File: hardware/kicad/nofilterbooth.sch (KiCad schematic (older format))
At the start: 2 parts

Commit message: kicad schematic & pcb v0.1
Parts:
- CONN_POWER_IN1: symbol nofilterbooth:Conn_01x02-Connector_Generic -> 1nofilterbooth:Conn_01x02-Connector_Generic
- U_STEP_DOWN_5V1: footprint kicadlib:D24V90F5 -> 1nofilterbooth:D24V90F5; symbol nofilterbooth:D24V90F5 -> 1nofilterbooth:D24V90F5
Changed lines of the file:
@@
 $EndSheet
 $Comp
-L nofilterbooth:Conn_01x02-Connector_Generic CONN_POWER_IN1
+L 1nofilterbooth:Conn_01x02-Connector_Generic CONN_POWER_IN1
 U 1 1 5E43D742
 P 4075 1075
@@
 $EndComp
 $Comp
-L nofilterbooth:+12V-power #PWR0123
+L 1nofilterbooth:+12V-power #PWR0123
 U 1 1 5E3BF560
 P 4075 1275
@@
 $EndComp
 $Comp
-L nofilterbooth:GND-power #PWR0124
+L 1nofilterbooth:GND-power #PWR0124
 U 1 1 5E3C03FE
 P 4175 1275
@@
 $EndComp
 $Comp
-L nofilterbooth:D24V90F5 U_STEP_DOWN_5V1
+L 1nofilterbooth:D24V90F5 U_STEP_DOWN_5V1
 U 1 1 5E3C0E82
 P 6000 1125
 F 0 "U_STEP_DOWN_5V1" H 5675 975 50  0000 C CNN
 F 1 "D24V90F5" H 5725 825 50  0000 C CNN
-F 2 "kicadlib:D24V90F5" H 6000 1125 50  0001 C CNN
+F 2 "1nofilterbooth:D24V90F5" H 6000 1125 50  0001 C CNN
 F 3 "" H 6000 1125 50  0001 C CNN
 	1    6000 1125
@@
 $EndComp
 $Comp
-L nofilterbooth:+5V-power #PWR0128
+L 1nofilterbooth:+5V-power #PWR0128
 U 1 1 5E3C178D
 P 6200 1225
@@
 $EndComp
 $Comp
-L nofilterbooth:GND-power #PWR0126
+L 1nofilterbooth:GND-power #PWR0126
 U 1 1 5E3C0BAF
 P 6200 1425
@@
 $EndComp
 $Comp
-L nofilterbooth:GND-power #PWR0125
+L 1nofilterbooth:GND-power #PWR0125
 U 1 1 5E3BFE89
 P 5200 1425
@@
 $EndSheet
 $Comp
-L nofilterbooth:+12V-power #PWR0127
+L 1nofilterbooth:+12V-power #PWR0127
 U 1 1 5E3DD7DE
 P 5200 1225

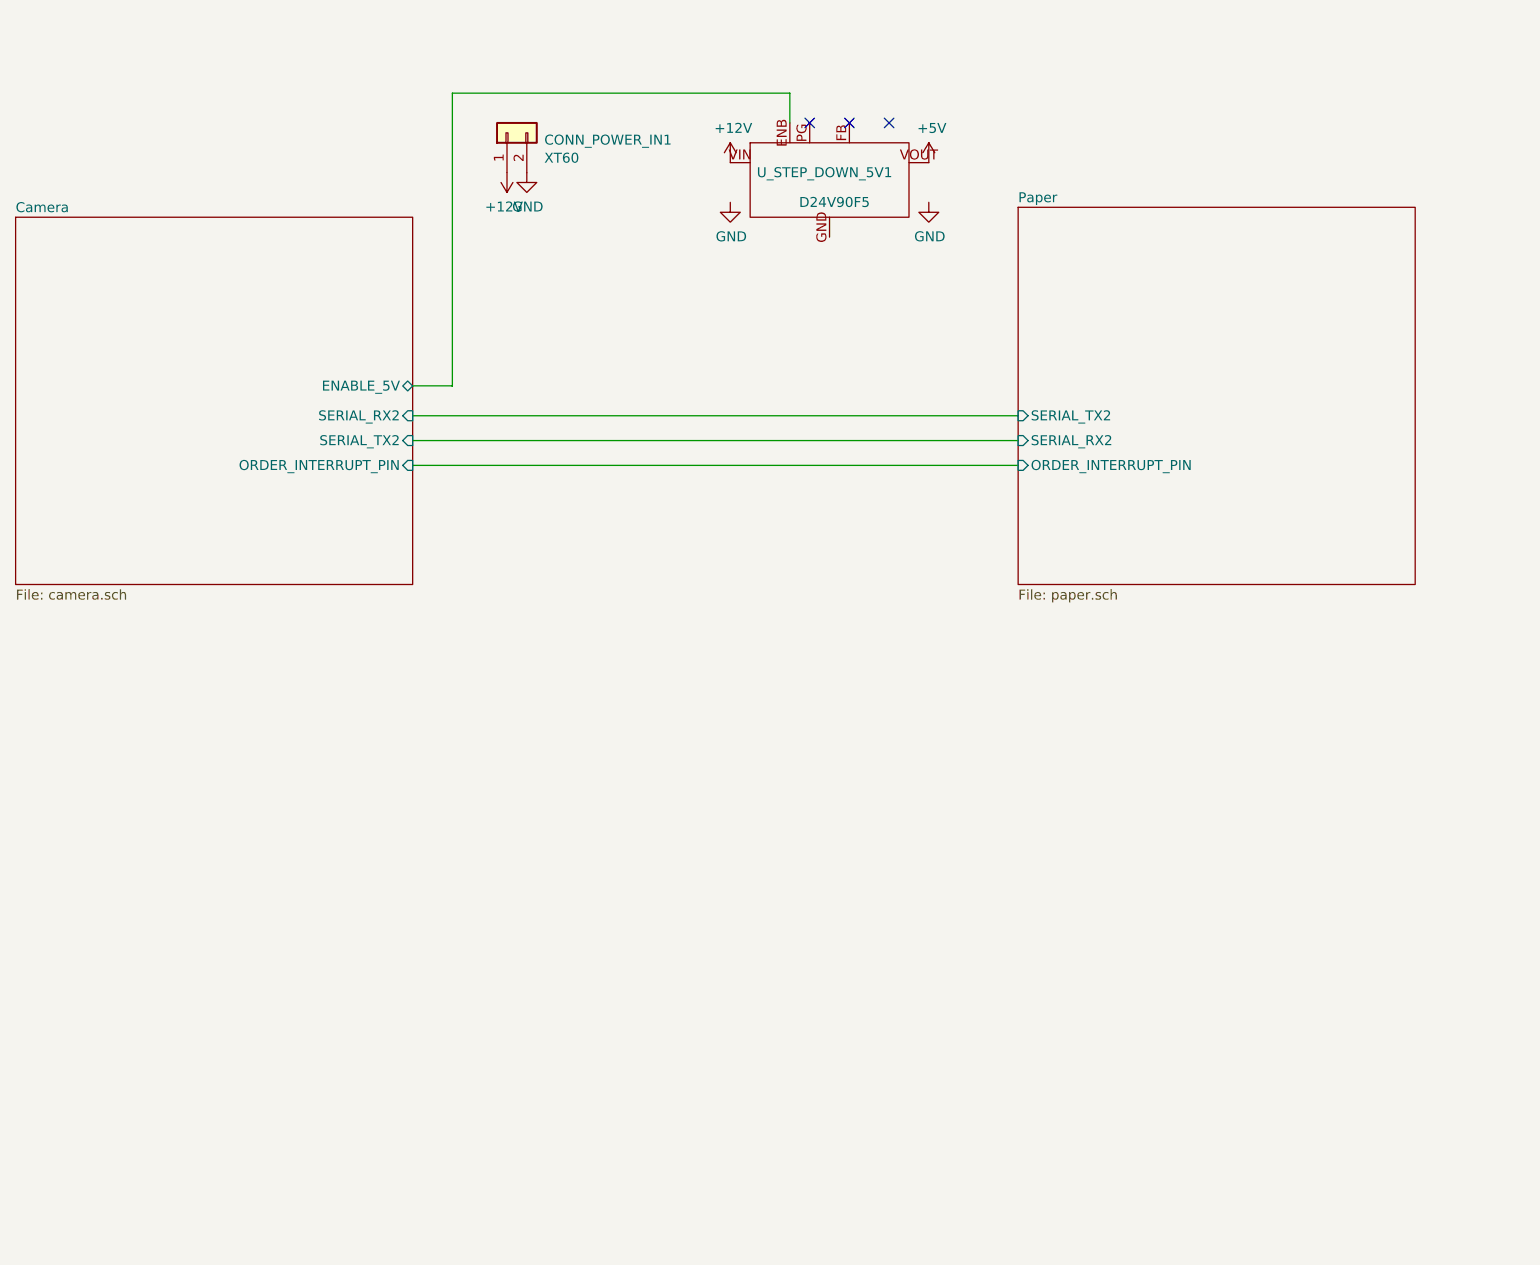
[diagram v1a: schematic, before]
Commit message: correction schematic gilou
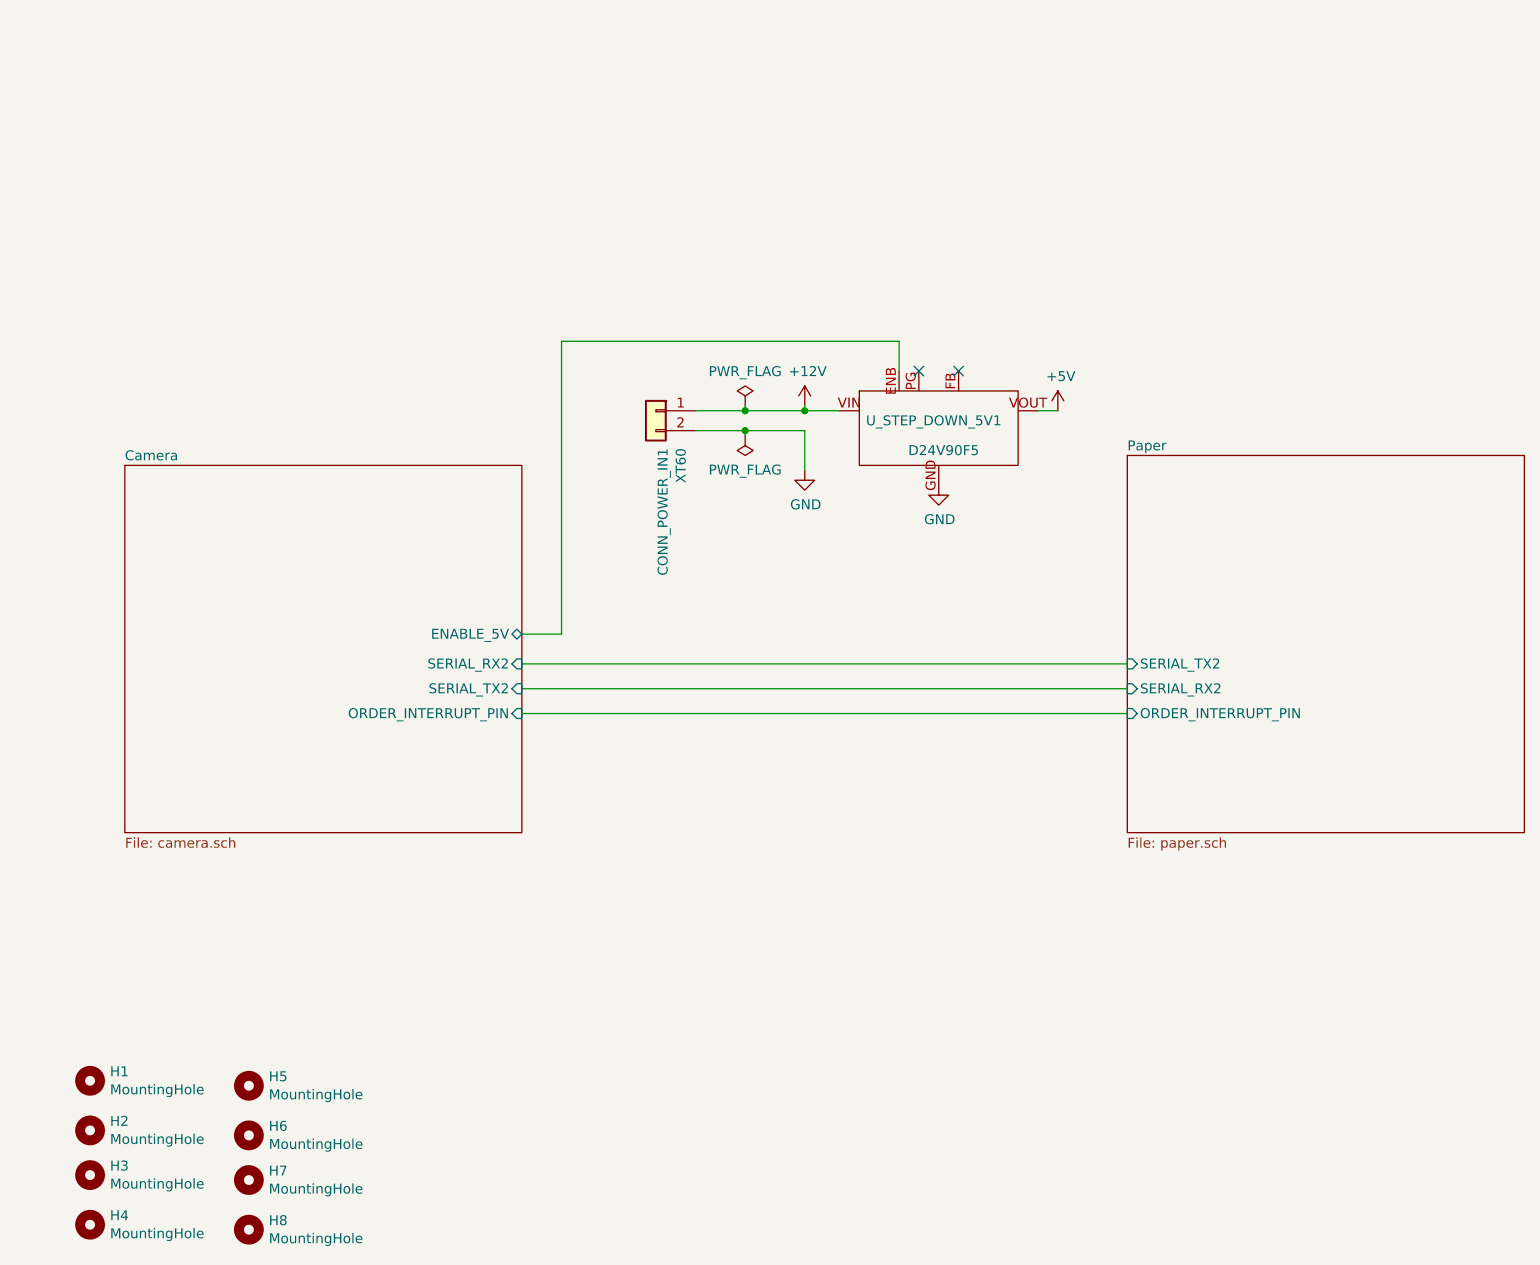
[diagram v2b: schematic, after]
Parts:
- added H1, H2, H3, H4, H5, H6, H7, H8: MountingHole, MountingHole:MountingHole_3.2mm_M3, symbol Mechanical:MountingHole
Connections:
- net GND: now also U_STEP_DOWN_5V1.GND
- no-connect marks 3 -> 2
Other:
- moved on the sheet: CONN_POWER_IN1, U_STEP_DOWN_5V1

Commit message: update, gilou dans la place
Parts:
- removed H5, H6, H7, H8: MountingHole, MountingHole:MountingHole_3.2mm_M3, symbol Mechanical:MountingHole
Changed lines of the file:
@@
 	1    0    0    -1
 $EndComp
-$Comp
-L Mechanical:MountingHole H5
-U 1 1 5E50E3A3
-P 2775 5875
-F 0 "H5" H 2875 5921 50  0000 L CNN
-F 1 "MountingHole" H 2875 5830 50  0000 L CNN
-F 2 "MountingHole:MountingHole_3.2mm_M3" H 2775 5875 50  0001 C CNN
-F 3 "~" H 2775 5875 50  0001 C CNN
-	1    2775 5875
-	1    0    0    -1
-$EndComp
-$Comp
-L Mechanical:MountingHole H6
-U 1 1 5E50E3A9
-P 2775 6125
-F 0 "H6" H 2875 6171 50  0000 L CNN
-F 1 "MountingHole" H 2875 6080 50  0000 L CNN
-F 2 "MountingHole:MountingHole_3.2mm_M3" H 2775 6125 50  0001 C CNN
-F 3 "~" H 2775 6125 50  0001 C CNN
-	1    2775 6125
-	1    0    0    -1
-$EndComp
-$Comp
-L Mechanical:MountingHole H7
-U 1 1 5E50E3AF
-P 2775 6350
-F 0 "H7" H 2875 6396 50  0000 L CNN
-F 1 "MountingHole" H 2875 6305 50  0000 L CNN
-F 2 "MountingHole:MountingHole_3.2mm_M3" H 2775 6350 50  0001 C CNN
-F 3 "~" H 2775 6350 50  0001 C CNN
-	1    2775 6350
-	1    0    0    -1
-$EndComp
-$Comp
-L Mechanical:MountingHole H8
-U 1 1 5E50E3B5
-P 2775 6600
-F 0 "H8" H 2875 6646 50  0000 L CNN
-F 1 "MountingHole" H 2875 6555 50  0000 L CNN
-F 2 "MountingHole:MountingHole_3.2mm_M3" H 2775 6600 50  0001 C CNN
-F 3 "~" H 2775 6600 50  0001 C CNN
-	1    2775 6600
-	1    0    0    -1
-$EndComp
+Text Label 5550 3750 0    50   ~ 0
+AtoB
+Text Label 5550 3875 0    50   ~ 0
+BtoA
 $EndSCHEMATC
